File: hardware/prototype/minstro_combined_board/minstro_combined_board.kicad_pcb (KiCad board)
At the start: 4 copper layers, 130 x 100 mm, 141 parts, among them J1001 VFO, J301 BATT, J401 BOOT, J403 USB_C_Receptacle_USB2.0_16P, J404 SDMMC 4b, J405 Conn_Coaxial, J501 Headset, J502 SPKR, J601 FT6236, J602 ILI9488, J603 ST7789, J701 SOICbite-SWD, J801 NAV CONN, Q601 2N7002, Q701 2N7002, SW401 RST, SW801 Navigation_Encoder_Joystick_S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, U201 LMR36006, U301 BQ24074RGT, U401 ESP32-S3, U402 W25Q128JVS, U701 ATSAMD10D13A-M, Y401 40 MHz

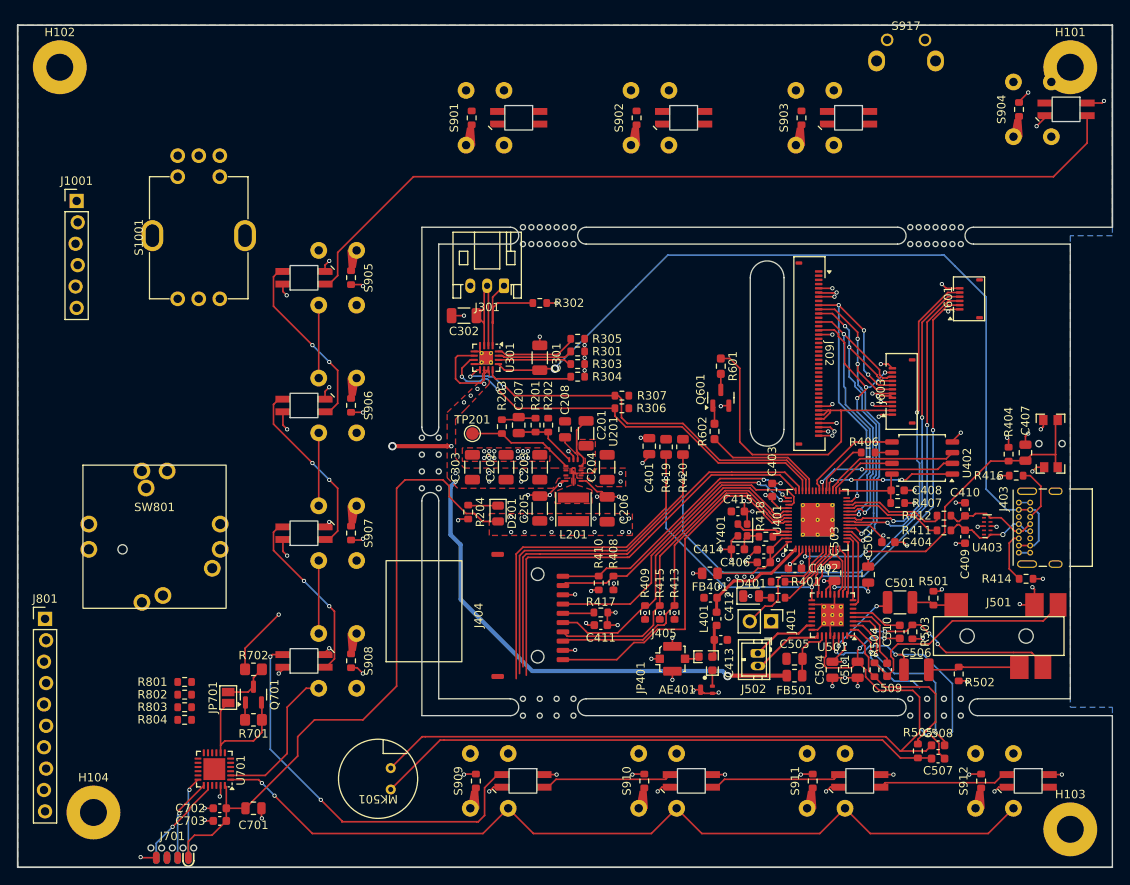
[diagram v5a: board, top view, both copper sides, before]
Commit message: PCB size fix started
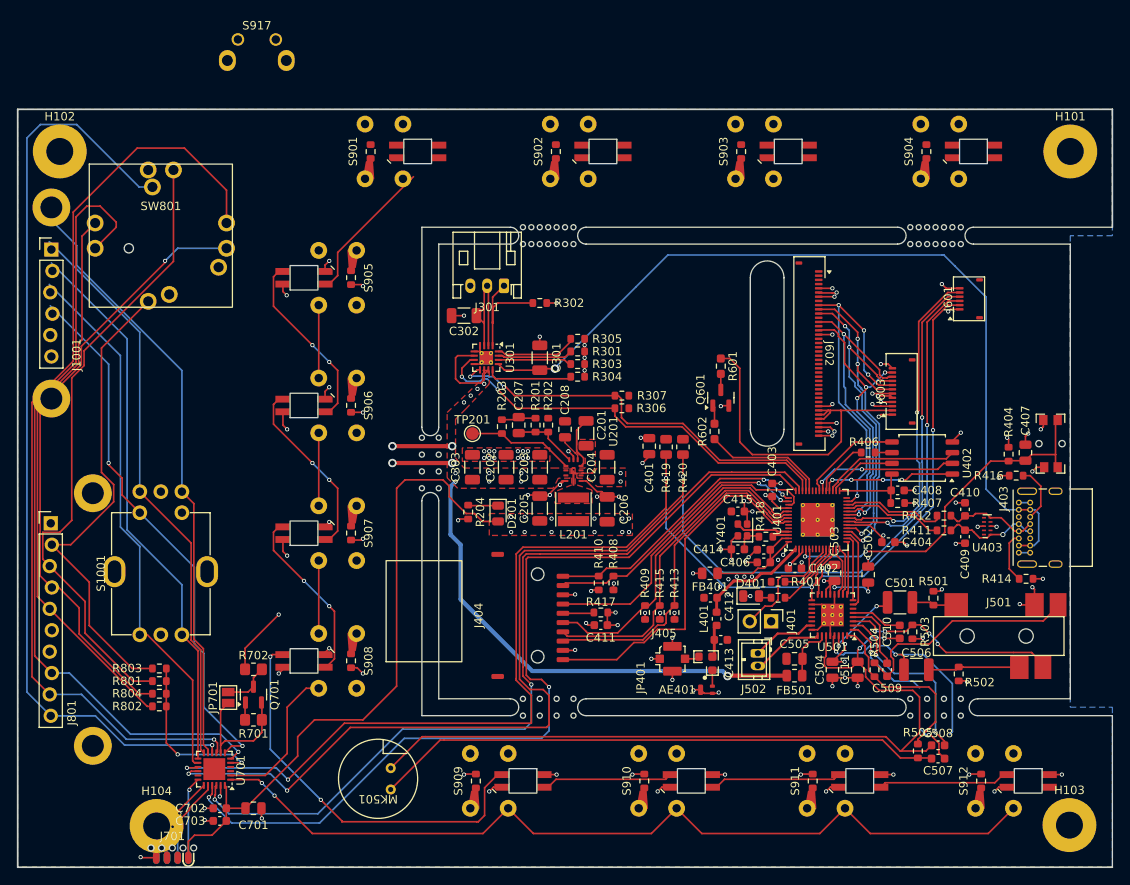
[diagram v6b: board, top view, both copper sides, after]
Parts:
- J1001: footprint BVH_PinHeader_FrictionRetention:PinHeader_1x06_P2.54mm_Vertical -> BVH_Connectors_Misc:Anchored_PinHeader_1x06_P2.54mm_Vertical_M2.5
- J801: footprint BVH_PinHeader_FrictionRetention:PinHeader_1x10_P2.54mm_Vertical -> BVH_Connectors_Misc:Anchored_Offset_PinHeader_1x10_P2.54mm_Vertical_M2.5
- moved S917 77.1 mm to (93.4, 43.0)
- moved S1001 40.2 mm to (82.0, 104.9)
- moved SW801 35.8 mm to (82.0, 65.0)
- moved S901 12.6 mm to (108.5, 55.0)
- moved S904 12.1 mm to (174.5, 55.0)
- moved J801 11.4 mm to (68.9, 99.2)
- moved S902 10.4 mm to (130.5, 55.0)
- moved H101 10.0 mm to (190.0, 55.0)
- moved H102 10.0 mm to (70.0, 55.0)
- moved S903 8.21 mm to (152.5, 55.0)
- moved H104 7.67 mm to (81.5, 135.1)
- moved J1001 6.50 mm to (69.0, 66.7)
- moved R803 5.49 mm to (81.8, 116.4)
- moved R804 4.31 mm to (81.8, 119.4)
- moved R802 3.31 mm to (81.8, 120.9)
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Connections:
- net Net-(J801-Pin_2) renamed /Nav Switch/Nav_Up_VD
- net Net-(J801-Pin_3) renamed /Nav Switch/Nav_Down_VD
- net Net-(J801-Pin_4) renamed /Nav Switch/Nav_Left_VD
- net Net-(J801-Pin_5) renamed /Nav Switch/Nav_Right_VD
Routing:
- net /HMI Controller/NAV_B: track 0.00 -> 111.0 mm, vias 0 -> 1
- net /HMI Controller/NAV_SW: track 0.00 -> 110.0 mm, vias 0 -> 1
- net /HMI Controller/NAV_A: track 0.00 -> 94.5 mm, vias 0 -> 1
- net Net-(S904B-DO): track 102.3 -> 17.4 mm
- net /Nav Switch/Nav_Down_VD: track 0.00 -> 75.0 mm
- net /Nav Switch/Nav_Left_VD: track 0.00 -> 72.4 mm, vias 0 -> 1
- net /HMI Controller/VFO_A: track 0.00 -> 70.9 mm
- net /HMI Controller/VFO_B: track 0.00 -> 68.3 mm
- net /Nav Switch/Nav_Right_VD: track 0.00 -> 66.3 mm
- net /HMI Controller/VFO_ADJ_A: track 0.00 -> 66.1 mm
- net /HMI Controller/VFO_ADJ_B: track 0.00 -> 64.9 mm
- net /HMI Controller/VFO_SW: track 0.00 -> 64.2 mm, vias 0 -> 2
- net /Nav Switch/Nav_Up_VD: track 0.00 -> 57.2 mm
- net /I2C_SCL: track 115.8 -> 172.4 mm, vias 3 -> 5
- net /ESP32 Microcontroller/HMI_INT: track 50.7 -> 107.2 mm, vias 0 -> 2
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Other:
- board size 130 x 100 mm -> 130 x 90 mm

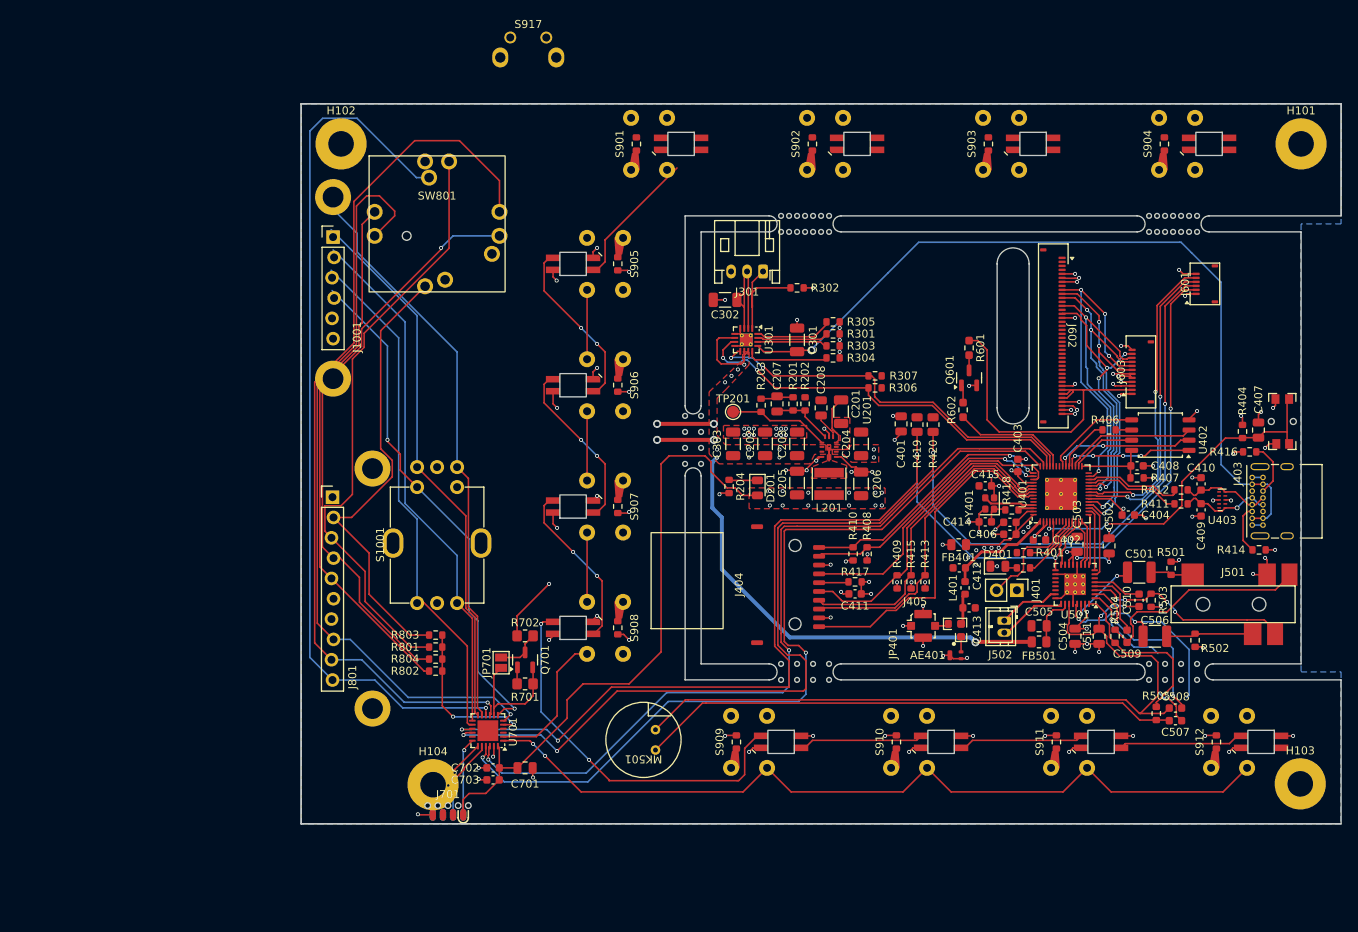
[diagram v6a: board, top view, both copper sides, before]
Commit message: Board resizing
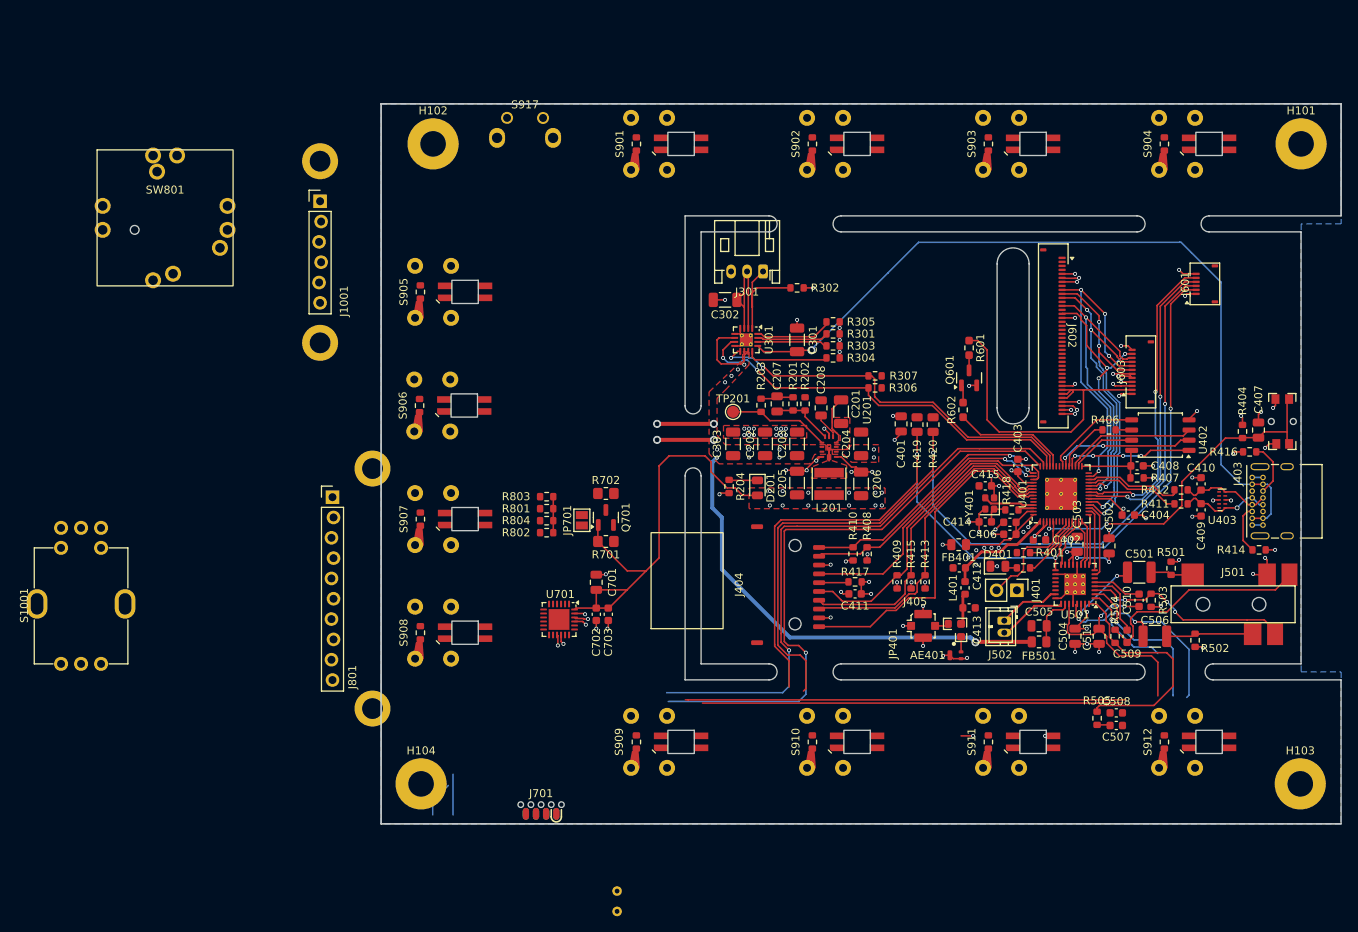
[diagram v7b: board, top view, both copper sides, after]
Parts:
- removed REF** (x2): Untitled, BVH_Features:MouseBite_2mm_7holes
- removed REF** (x3): Untitled, BVH_Features:MouseBite_2mm_4holes_Wide
- MK501: moved to B.Cu
- moved S1001 45.1 mm to (37.5, 112.5)
- moved SW801 34.0 mm to (48.0, 64.2)
- moved C703 25.2 mm to (103.4, 113.8), turned to -90 degrees
- moved C701 24.8 mm to (101.9, 109.8), turned to 90 degrees
- moved C702 23.1 mm to (101.9, 113.8), turned to -90 degrees
- moved R801 22.2 mm to (95.7, 100.6)
- moved R802 22.2 mm to (95.7, 103.6)
- moved R803 22.2 mm to (95.7, 99.1)
- moved R804 22.2 mm to (95.7, 102.1)
- moved S905 21.8 mm to (81.5, 73.5), turned to -90 degrees
- moved S906 21.7 mm to (81.4, 87.7), turned to -90 degrees
- moved S907 21.6 mm to (81.5, 101.9), turned to -90 degrees
- moved S908 21.5 mm to (81.5, 116.1), turned to -90 degrees
- moved MK501 20.7 mm to (103.0, 149.7)
- moved JP701 20.5 mm to (100.1, 102.0)
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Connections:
- U701 pad 2: /HMI Controller/ROW_B -> /HMI Controller/ROW_A
- U701 pad 3: unconnected-(U701-PA04-Pad3) -> /HMI Controller/RGB_DATA_3.3
- U701 pad 4: /HMI Controller/ROW_A -> /HMI Controller/NAV_DIR
- U701 pad 5: /HMI Controller/NAV_DIR -> /HMI Controller/NAV_A
- U701 pad 6: /HMI Controller/NAV_A -> /HMI Controller/ROW_B
- U701 pad 8: /HMI Controller/RGB_DATA_3.3 -> unconnected-(U701-PA09/XOUT-Pad8)
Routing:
- net /HMI Controller/NAV_B: track 111.0 -> 0.00 mm, vias 1 -> 0
- net /HMI Controller/NAV_SW: track 110.0 -> 0.00 mm, vias 1 -> 0
- net /HMI Controller/ROW_C: track 104.3 -> 0.00 mm, vias 2 -> 0
- net /HMI Controller/NAV_A: track 94.5 -> 0.00 mm, vias 1 -> 0
- net /Nav Switch/Nav_Down_VD: track 75.0 -> 0.00 mm
- net /Nav Switch/Nav_Left_VD: track 72.4 -> 0.00 mm, vias 1 -> 0
- net /HMI Controller/VFO_A: track 70.9 -> 0.00 mm
- net /HMI Controller/VFO_B: track 68.3 -> 0.00 mm
- net /Nav Switch/Nav_Right_VD: track 66.3 -> 0.00 mm
- net /HMI Controller/VFO_ADJ_A: track 66.1 -> 0.00 mm
- net /Audio/Mic_P: track 67.6 -> 1.66 mm
- net /HMI Controller/VFO_ADJ_B: track 64.9 -> 0.00 mm
- net /HMI Controller/VFO_SW: track 64.2 -> 0.00 mm, vias 2 -> 0
- net /Nav Switch/Nav_Up_VD: track 57.2 -> 0.00 mm
- net Net-(S908B-DO): track 48.0 -> 0.00 mm, vias 2 -> 0
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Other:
- board size 130 x 90 mm -> 120 x 90 mm

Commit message: Layout completed, initial review
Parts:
- removed S1001: ~, BVH_Switches:Alps_EC11E_Dual_Shaft_Rotary_Encoder_With_Switch
- removed SW801: Navigation_Encoder_Joystick_Switch, BVH_Switches:RKJXT1F42001_Navigation_Switch
- added J402: I2C, BVH_PinHeader_FrictionRetention:PinHeader_1x04_P2.54mm_Vertical, F.Cu at (143.5, 73.7)
- added J702: Conn_ARM_JTAG_SWD_10, BVH_Connectors_Misc:Cortex_Debug_PinSocket_2x05_P1.27mm_Vertical_SMD, F.Cu at (89.8, 130.6)
- added REF**: Untitled, BVH_Features:MouseBite_2mm_4holes_Wide, F.Cu at (174.0, 65.0)
- added REF**: Untitled, BVH_Features:MouseBite_2mm_4holes_Wide, F.Cu at (128.0, 121.0)
- added REF**: Untitled, BVH_Features:MouseBite_2mm_4holes_Wide, F.Cu at (128.0, 65.0)
- added REF**: Untitled, BVH_Features:MouseBite_2mm_4holes_Wide, F.Cu at (114.0, 92.0)
- added REF**: Untitled, BVH_Features:MouseBite_2mm_4holes_Wide, F.Cu at (174.0, 121.0)
- J1001: footprint BVH_Connectors_Misc:Anchored_PinHeader_1x06_P2.54mm_Vertical_M2.5 -> BVH_PinHeader_FrictionRetention:PinHeader_1x06_P2.54mm_Vertical
- J801: footprint BVH_Connectors_Misc:Anchored_Offset_PinHeader_1x10_P2.54mm_Vertical_M2.5 -> BVH_PinHeader_FrictionRetention:PinHeader_1x10_P2.54mm_Vertical
- U701: footprint Package_DFN_QFN:QFN-24-1EP_4x4mm_P0.5mm_EP2.6x2.6mm -> Package_DFN_QFN:QFN-24-1EP_4x4mm_P0.5mm_EP2.6x2.6mm_ThermalVias
- moved J1001 28.8 mm to (94.9, 70.8)
- moved J801 23.6 mm to (91.9, 93.9)
- moved MK501 21.1 mm to (99.0, 129.0)
- moved C508 10.3 mm to (171.9, 117.1), turned to -90 degrees
- moved J701 6.33 mm to (89.0, 137.9)
- moved R502 4.75 mm to (181.5, 117.0)
- moved C506 4.30 mm to (176.0, 117.0)
- moved C507 4.03 mm to (168.5, 124.0)
- moved R505 3.40 mm to (162.0, 124.5), turned to 90 degrees
- moved H104 1.50 mm to (81.5, 135.0)
- moved AE401 0.33 mm to (146.8, 118.6)
- moved C402 0.20 mm to (157.5, 104.5)
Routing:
- net /HMI Controller/ROW_A: track 0.00 -> 128.6 mm, vias 0 -> 1
- net Net-(S904B-DO): track 0.00 -> 109.3 mm
- net /HMI Controller/ROW_C: track 0.00 -> 96.5 mm, vias 0 -> 4
- net /HMI Controller/POW_SW: track 0.00 -> 69.3 mm, vias 0 -> 1
- net /Audio/Mic_P: track 1.66 -> 69.0 mm
- net +3.3V: track 121.9 -> 178.0 mm, vias 41 -> 47
- net /HMI Controller/RGB_DATA: track 0.00 -> 53.4 mm, vias 0 -> 2
- net Net-(S908B-DO): track 0.00 -> 51.1 mm
- net /I2C_SDA: track 126.2 -> 175.9 mm, vias 4 -> 5
- net /I2C_SCL: track 125.9 -> 175.4 mm, vias 4 -> 5
- net /HMI Controller/VFO_A: track 0.00 -> 48.7 mm, vias 0 -> 1
- net /HMI Controller/VFO_B: track 0.00 -> 44.8 mm, vias 0 -> 1
- net /HMI Controller/VFO_ADJ_A: track 0.00 -> 41.8 mm, vias 0 -> 1
- net /HMI Controller/VFO_ADJ_B: track 0.00 -> 39.5 mm, vias 0 -> 1
- net /HMI Controller/SWCLK: track 0.00 -> 38.2 mm, vias 0 -> 3
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- added copper zone on F.Cu, net /ESP32 Microcontroller/VDD33A
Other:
- outline, holes or cut-outs redrawn
